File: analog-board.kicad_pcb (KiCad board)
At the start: 2 copper layers, 200 x 150 mm, 497 parts, among them J1 AC IN, J2 OUT, J3 CONN_20X2, P2 CONN_01X02, Q1 2N3906, Q10 2N3906, Q11 2N3906, Q12 2N3906, Q13 2N3906, Q14 2N3906, Q15 2N3906, Q16 2N3906, Q17 NPN, Q18 NPN, Q19 J111, Q2 2N3906, Q20 2N3906, Q3 2N3906, Q4 2N3906, Q5 2N3906, Q6 BCM857BS, Q7 2N3906, Q8 2N3906, Q9 2N3906, U1 LM13700, U10 ADR01, U11 DG212B, U12 DG212B, U13 DG408, U14 DG408, U15 TL072-, U16 DG408, U17 DG408, U18 LM13700, U19 LM13700, U2 LM13700, U20 74HC75, U21 TL072-, U22 TL074-, U23 TL074-, U24 TL074-, U25 TL074-, U26 TL072-, U27 TL074-, U28 TL074-, U29 LM13700, U3 LM13700, U30 LM13700, U31 TL074-, U32 LM13700, U33 TL074-, U34 TL074-, U35 TL074-, U36 74LV573, U38 0 - 10V, U39 TL074-, U4 DG212B, U40 DG419, U41 0 - 10V, U42 10 - 0V, U43 LM7812, U44 LM7912, U45 DG408, U46 7805, U5 TL074-, U6 AD5556, U7 TL072-, U8 TL074-, U9 AD8672

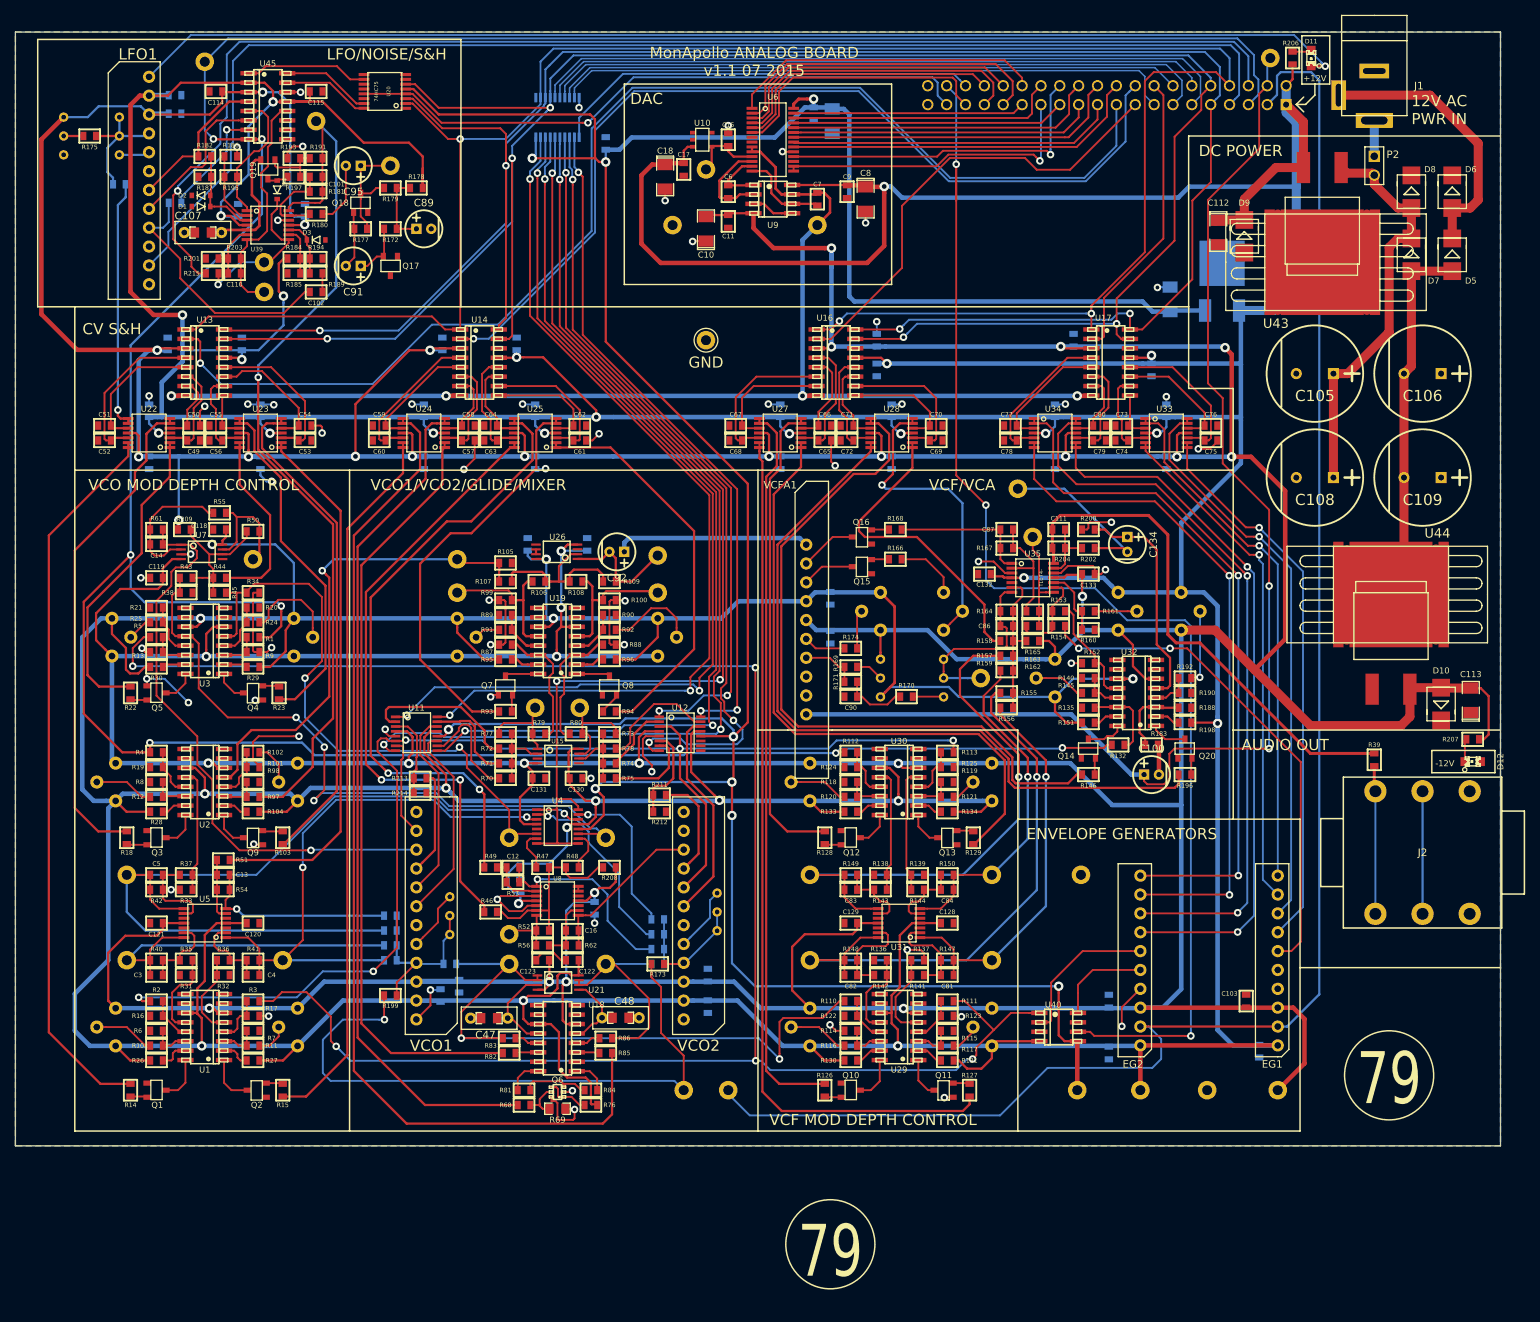
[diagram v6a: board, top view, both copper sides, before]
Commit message: routed tune comparator
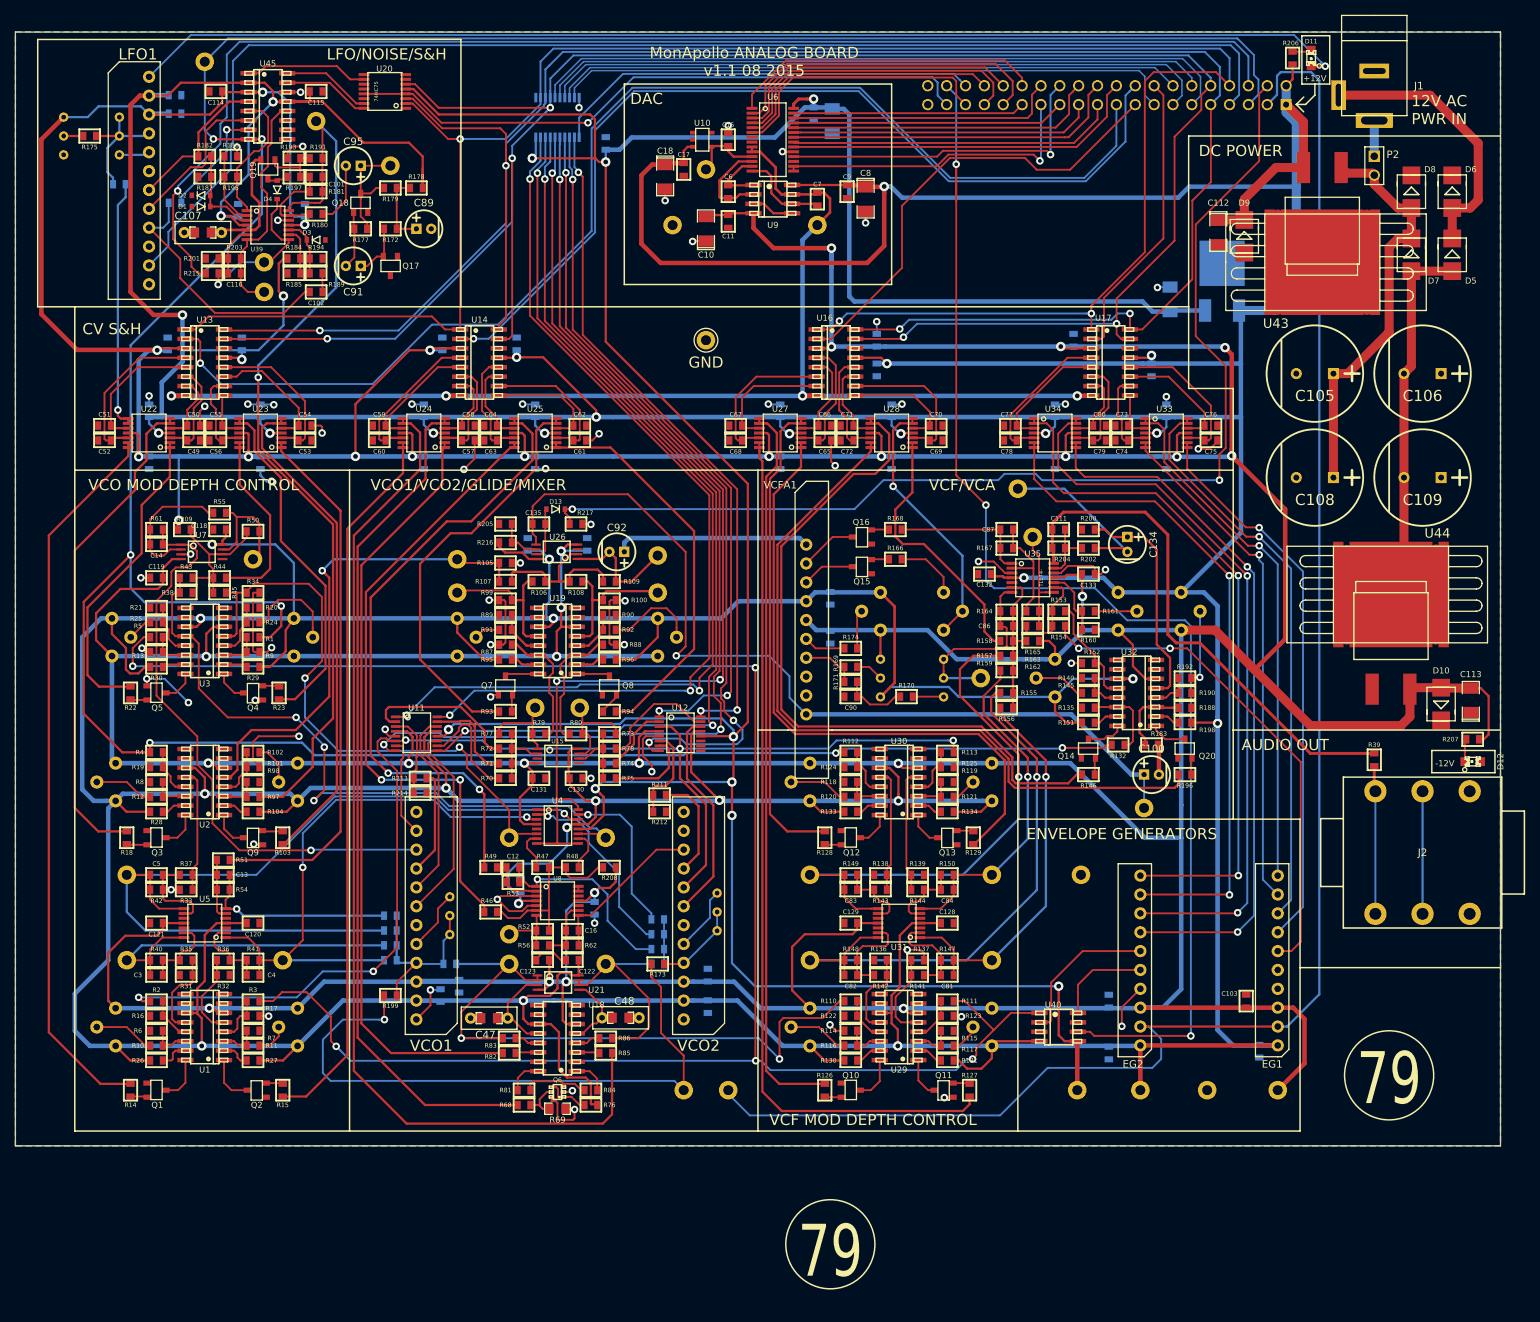
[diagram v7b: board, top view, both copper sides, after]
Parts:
- added C135: 10p, MyModules:SM0603-C-JRL, F.Cu at (70.5, 66.2)
- added D13: 1N4148, MyModules:SOD323-JRL, F.Cu at (72.8, 64.2)
- added R205: 10K, MyModules:SM0603-R-JRL, F.Cu at (66.0, 66.2)
- added R216: 270K, MyModules:SM0603-R-JRL, F.Cu at (66.0, 68.8)
- added R217: 22K, MyModules:SM0603-R-JRL, F.Cu at (75.5, 66.2)
- moved TP24 102.4 mm to (152.0, 104.5)
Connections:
- C100 pad 1: TUNE -> Net-(C100-Pad1)
- TP24 pad 1: TUNE -> Net-(C100-Pad1)
- U26 pad 5: GND -> Net-(C100-Pad1)
- U26 pad 6: Net-(U26-Pad6) -> Net-(R205-Pad1)
- U26 pad 7: Net-(U26-Pad6) -> Net-(C135-Pad2)
- VCFA1 pad 10: TUNE -> Net-(C100-Pad1)
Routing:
- net Net-(C100-Pad1): track 0.00 -> 120.2 mm, vias 0 -> 1
- net TUNE: track 170.6 -> 151.9 mm
- net Net-(C135-Pad2): track 0.00 -> 7.09 mm
- net +12V: track 1609.7 -> 1616.5 mm
- net CUTOFF CV: track 42.2 -> 35.7 mm
- net RES CV: track 41.6 -> 35.5 mm
- net Net-(R205-Pad1): track 0.00 -> 6.14 mm
- net GND: track 368.8 -> 366.4 mm, vias 63 -> 64
- net Net-(U26-Pad6): track 0.65 -> 0.00 mm
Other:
- board text added: "GATE OUT"
- board text added: "MonApollo ANALOG BOARD v1.1 08 2015"
- board text removed: "GATE IN"
- board text removed: "MonApollo ANALOG BOARD v1.1 07 2015"
